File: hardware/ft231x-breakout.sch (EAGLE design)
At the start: 27 parts, among them Q1 2N7002PW, U1 FT231XS

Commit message: Silk Change
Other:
- note added: "V01"
- note removed: "V10"
- moved on the sheet: JP1, JP10, JP11

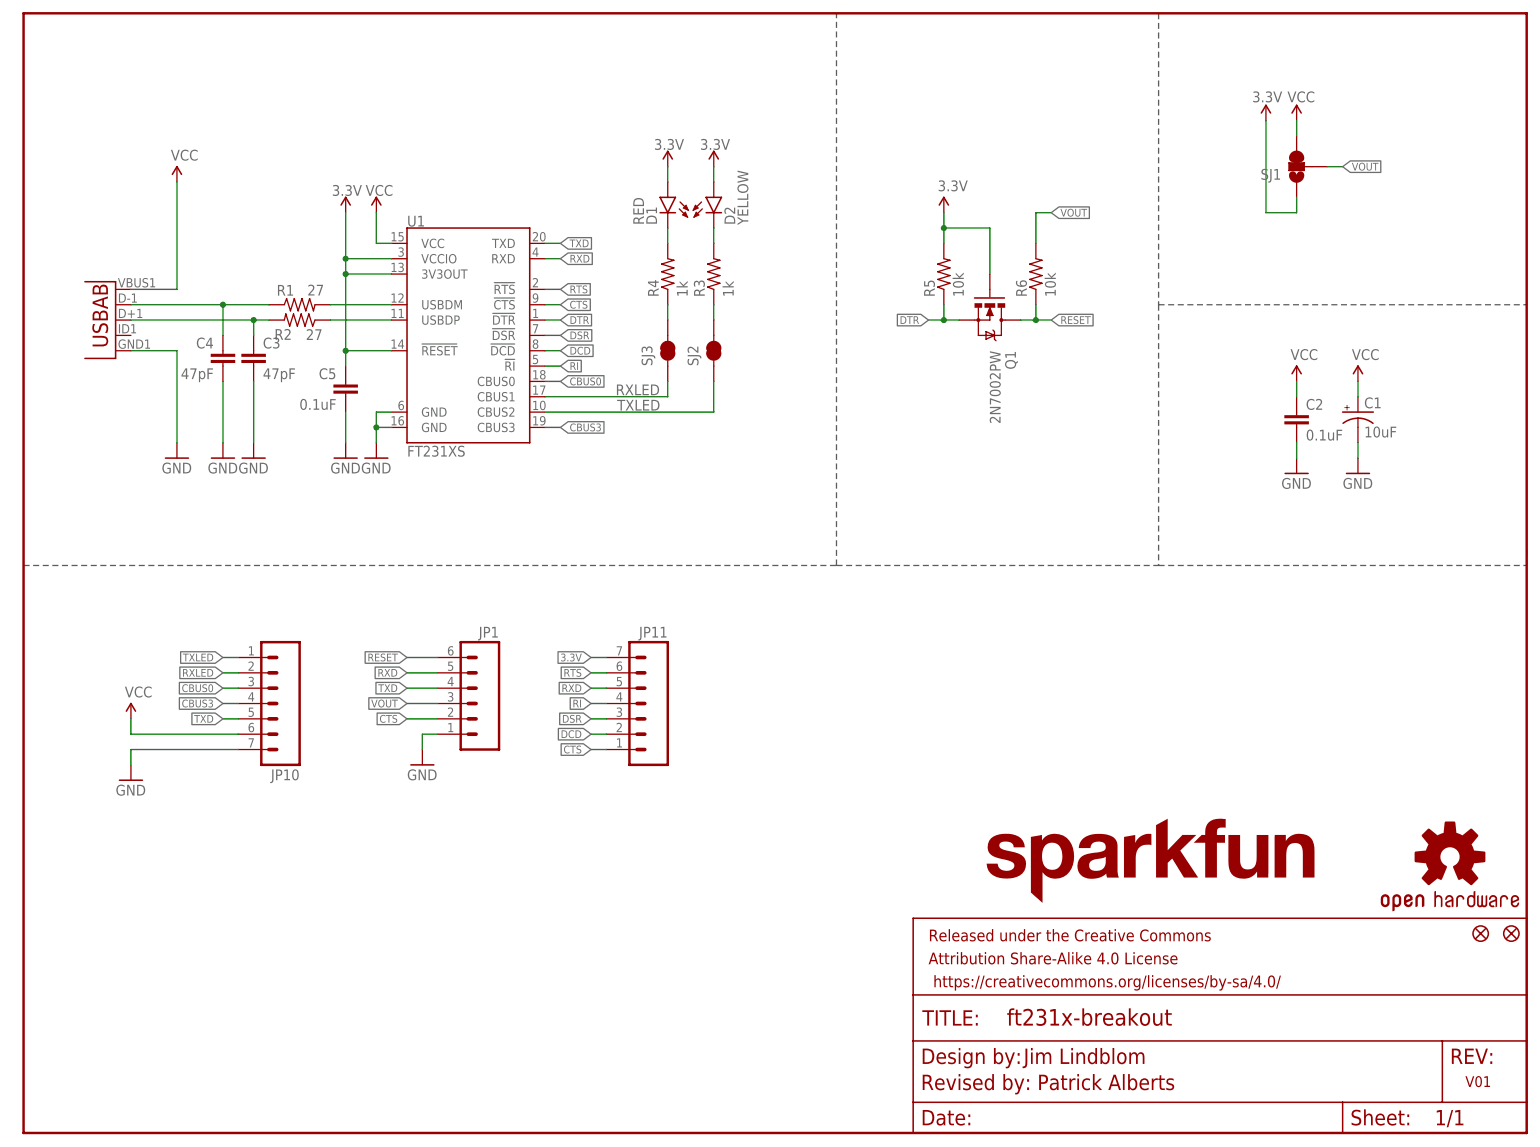
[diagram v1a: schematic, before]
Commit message: Adding sch notes, small silk edits, small trace fix
Adding notes for VIN and jumper usage. Also made some small silk edits
to avoid silk getting cut off by vias. Had to make one small trace
change on 3.3V net to avoid natural bridge between pads 13 and 14.
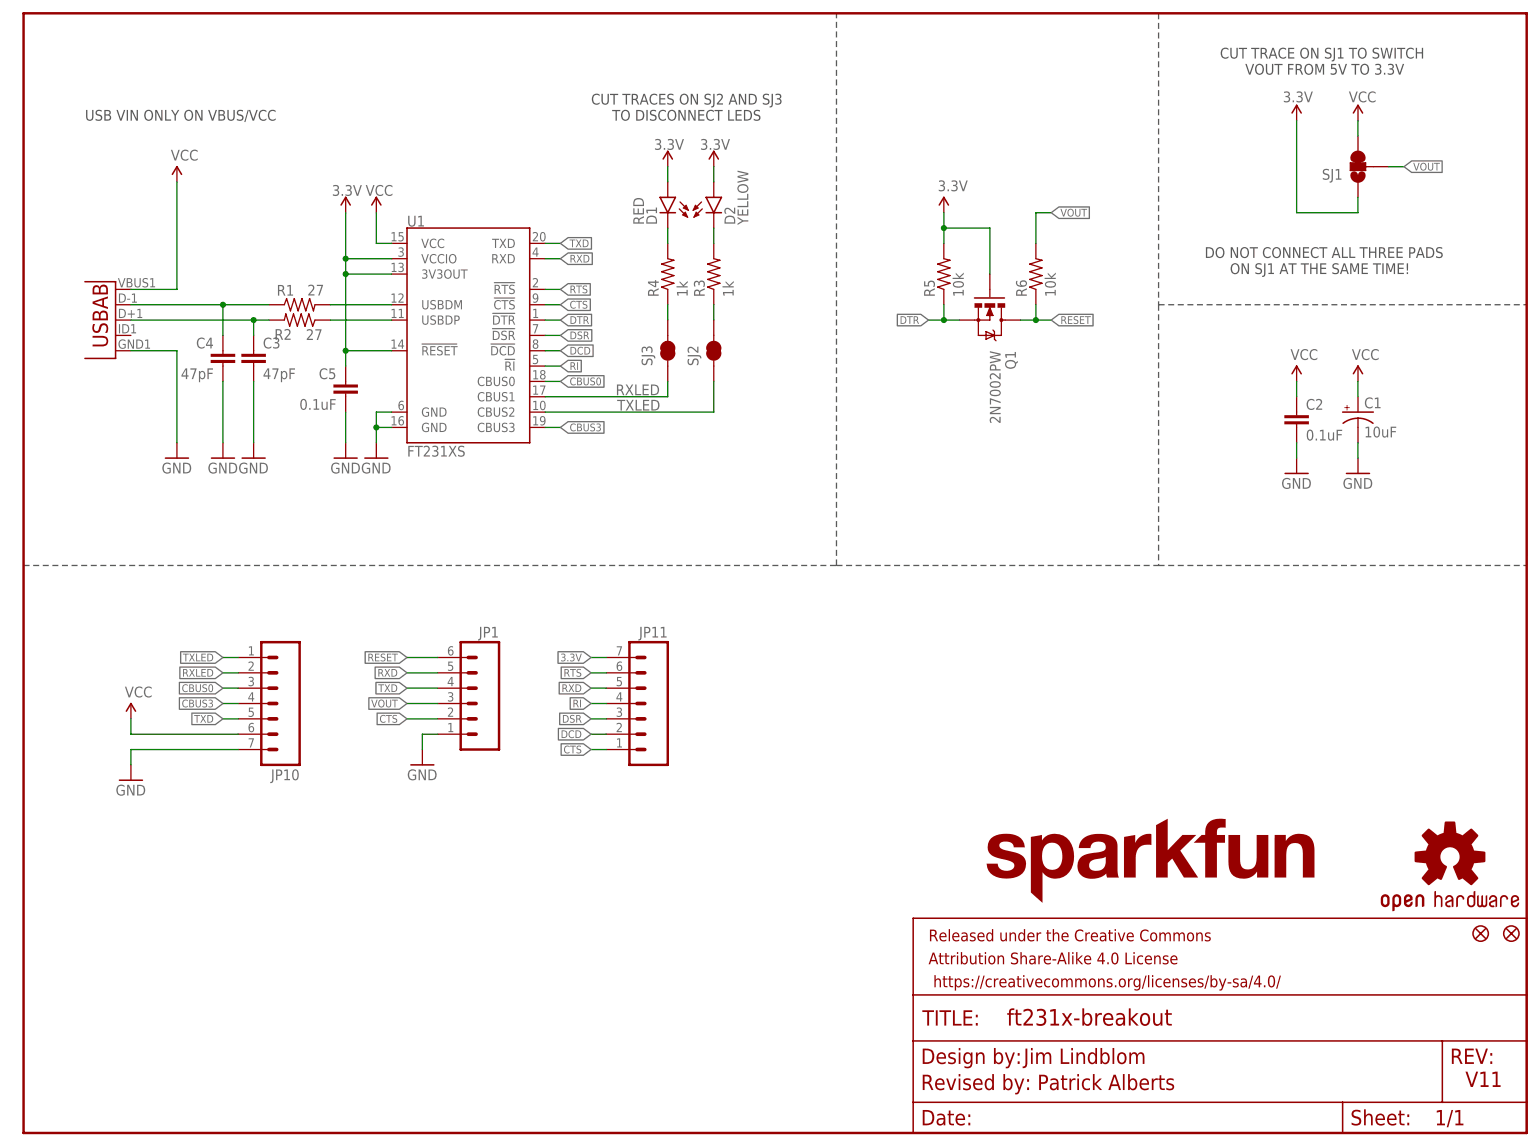
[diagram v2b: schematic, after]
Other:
- note added: "CUT TRACE ON SJ1 TO SWITCH VOUT FROM 5V TO 3.3V"
- note added: "CUT TRACES ON SJ2 AND SJ3 TO DISCONNECT LEDS"
- note added: "DO NOT CONNECT ALL THREE PADS ON SJ1 AT THE SAME TIME!"
- note added: "USB VIN ONLY ON VBUS/VCC"
- note added: "V11"
- note removed: "V01"
- moved on the sheet: SJ1
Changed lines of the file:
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@@
 <sheet>
 <plain>
-<wire x1="210.82" y1="160.02" x2="210.82" y2="161.798" width="1.016" layer="94"/>
+<wire x1="220.98" y1="160.02" x2="220.98" y2="161.798" width="1.016" layer="94"/>
 <wire x1="114.3" y1="128.778" x2="114.3" y2="130.302" width="1.016" layer="94"/>
 <wire x1="106.68" y1="128.778" x2="106.68" y2="130.302" width="1.016" layer="94"/>
@@
 <wire x1="187.96" y1="93.98" x2="248.92" y2="93.98" width="0.127" layer="97" style="shortdash"/>
 <wire x1="248.92" y1="93.98" x2="248.92" y2="96.52" width="0.127" layer="97" style="shortdash"/>
-<text x="238.76" y="7.62" size="1.778" layer="94">V01</text>
+<text x="238.76" y="7.62" size="2.54" layer="94">V11</text>
 <text x="165.608" y="11.43" size="2.54" layer="94">Jim Lindblom</text>
 <text x="148.59" y="7.112" size="2.54" layer="94">Revised by: Patrick Alberts</text>
 <wire x1="187.96" y1="137.16" x2="248.92" y2="137.16" width="0.127" layer="97" style="shortdash"/>
+<text x="10.16" y="167.64" size="1.778" layer="97">USB VIN ONLY ON VBUS/VCC</text>
+<text x="93.98" y="167.64" size="1.778" layer="97">CUT TRACES ON SJ2 AND SJ3
+     TO DISCONNECT LEDS</text>
+<text x="198.12" y="175.26" size="1.778" layer="97">CUT TRACE ON SJ1 TO SWITCH
+      VOUT FROM 5V TO 3.3V</text>
+<text x="195.58" y="142.24" size="1.778" layer="97">DO NOT CONNECT ALL THREE PADS
+      ON SJ1 AT THE SAME TIME!</text>
 </plain>
 <instances>
@@
 <instance part="JP1" gate="G$1" x="73.66" y="71.12" rot="MR0"/>
 <instance part="GND8" gate="1" x="66.04" y="60.96"/>
-<instance part="SJ1" gate="G$1" x="210.82" y="160.02" rot="R180"/>
+<instance part="SJ1" gate="G$1" x="220.98" y="160.02" rot="R180"/>
 <instance part="P+5" gate="G$1" x="53.34" y="152.4" smashed="yes">
 <attribute name="VALUE" x="51.054" y="155.194" size="1.778" layer="96"/>
 </instance>
-<instance part="P+6" gate="G$1" x="210.82" y="167.64" smashed="yes">
-<attribute name="VALUE" x="209.296" y="170.688" size="1.778" layer="96"/>
-</instance>
-<instance part="P+7" gate="G$1" x="205.74" y="167.64" smashed="yes">
-<attribute name="VALUE" x="203.454" y="170.688" size="1.778" layer="96"/>
+<instance part="P+6" gate="G$1" x="220.98" y="167.64" smashed="yes">
+<attribute name="VALUE" x="219.456" y="170.688" size="1.778" layer="96"/>
+</instance>
+<instance part="P+7" gate="G$1" x="210.82" y="167.64" smashed="yes">
+<attribute name="VALUE" x="208.534" y="170.688" size="1.778" layer="96"/>
 </instance>
 <instance part="P+1" gate="G$1" x="25.4" y="157.48"/>
@@
 <pinref part="SJ1" gate="G$1" pin="3"/>
 <pinref part="P+6" gate="G$1" pin="VCC"/>
-<wire x1="210.82" y1="167.64" x2="210.82" y2="165.1" width="0.1524" layer="91"/>
+<wire x1="220.98" y1="167.64" x2="220.98" y2="165.1" width="0.1524" layer="91"/>
 </segment>
 <segment>
@@
 <segment>
 <pinref part="SJ1" gate="G$1" pin="1"/>
-<wire x1="210.82" y1="154.94" x2="210.82" y2="152.4" width="0.1524" layer="91"/>
+<wire x1="220.98" y1="154.94" x2="220.98" y2="152.4" width="0.1524" layer="91"/>
 <pinref part="P+7" gate="G$1" pin="3.3V"/>
-<wire x1="210.82" y1="152.4" x2="205.74" y2="152.4" width="0.1524" layer="91"/>
-<wire x1="205.74" y1="152.4" x2="205.74" y2="167.64" width="0.1524" layer="91"/>
+<wire x1="220.98" y1="152.4" x2="210.82" y2="152.4" width="0.1524" layer="91"/>
+<wire x1="210.82" y1="152.4" x2="210.82" y2="167.64" width="0.1524" layer="91"/>
 </segment>
 <segment>
@@
 <segment>
 <pinref part="SJ1" gate="G$1" pin="2"/>
-<wire x1="215.9" y1="160.02" x2="218.44" y2="160.02" width="0.1524" layer="91"/>
-<label x="218.44" y="160.02" size="1.27" layer="95" xref="yes"/>
+<wire x1="226.06" y1="160.02" x2="228.6" y2="160.02" width="0.1524" layer="91"/>
+<label x="228.6" y="160.02" size="1.27" layer="95" xref="yes"/>
 </segment>
 <segment>
@@
 </schematic>
 </drawing>
+<compatibility>
+<note version="6.3" minversion="6.2.2" severity="warning">
+Since Version 6.2.2 text objects can contain more than one line,
+which will not be processed correctly with this version.
+</note>
+</compatibility>
 </eagle>

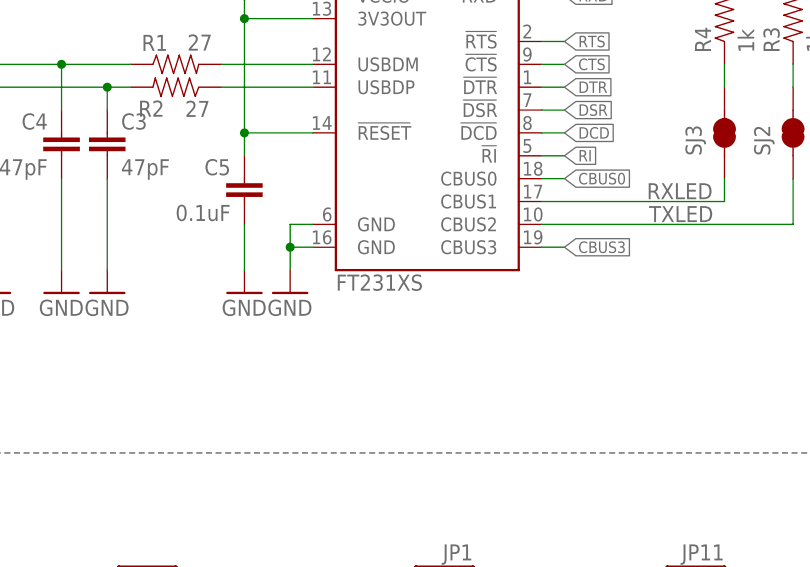
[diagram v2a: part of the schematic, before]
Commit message: Via drills change, moved R6 and library package update
Dropped all vias excepting the 3 usb connector staking vias to 15 mil to
jive better with silk. Moved R6 further in from edge of board to avoid
DPN damage/danger. Ran library update to include polarity mark silk
edits to SSOP20 package. Bumped micro-fiducials up to full fiducial
size.
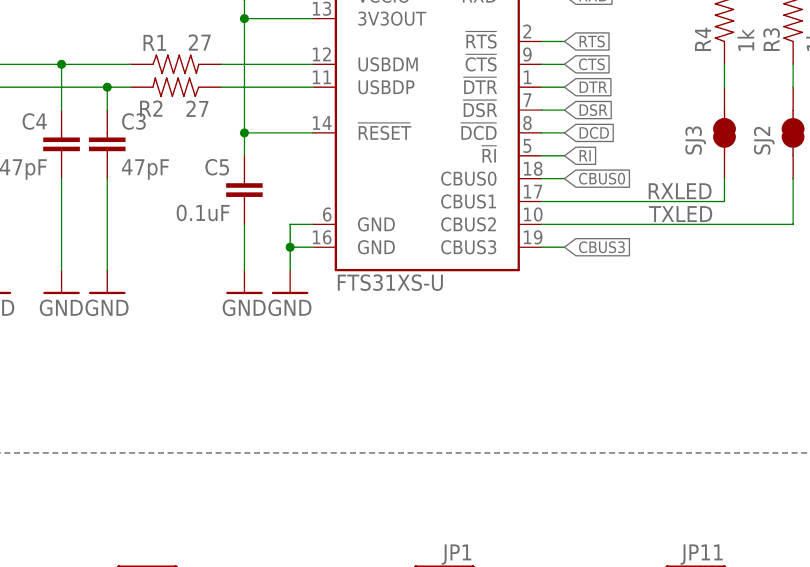
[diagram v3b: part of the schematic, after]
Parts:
- JP3, JP4: value FIDUCIALUFIDUCIAL -> FIDUCIAL1X2; device SparkFun-Aesthetics:FIDUCIALUFIDUCIAL -> SparkFun-Aesthetics:FIDUCIAL1X2
- U1: value FT231XS -> FTS31XS-U

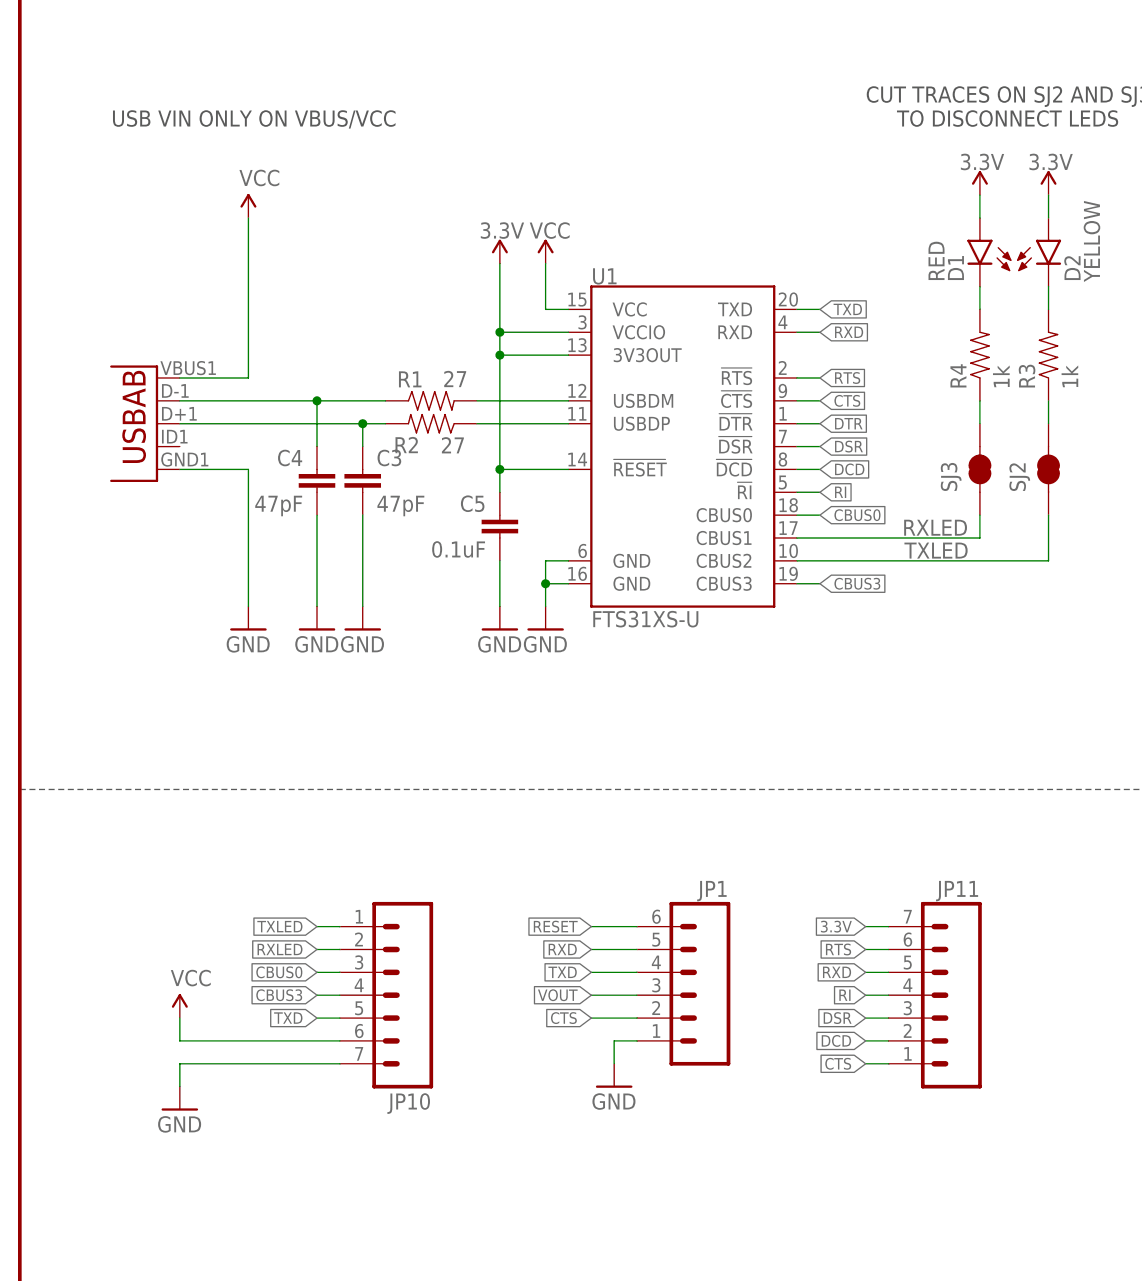
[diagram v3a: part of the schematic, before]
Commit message: Fixing issues from design checklist
See issue #4 in repo for full rundown.
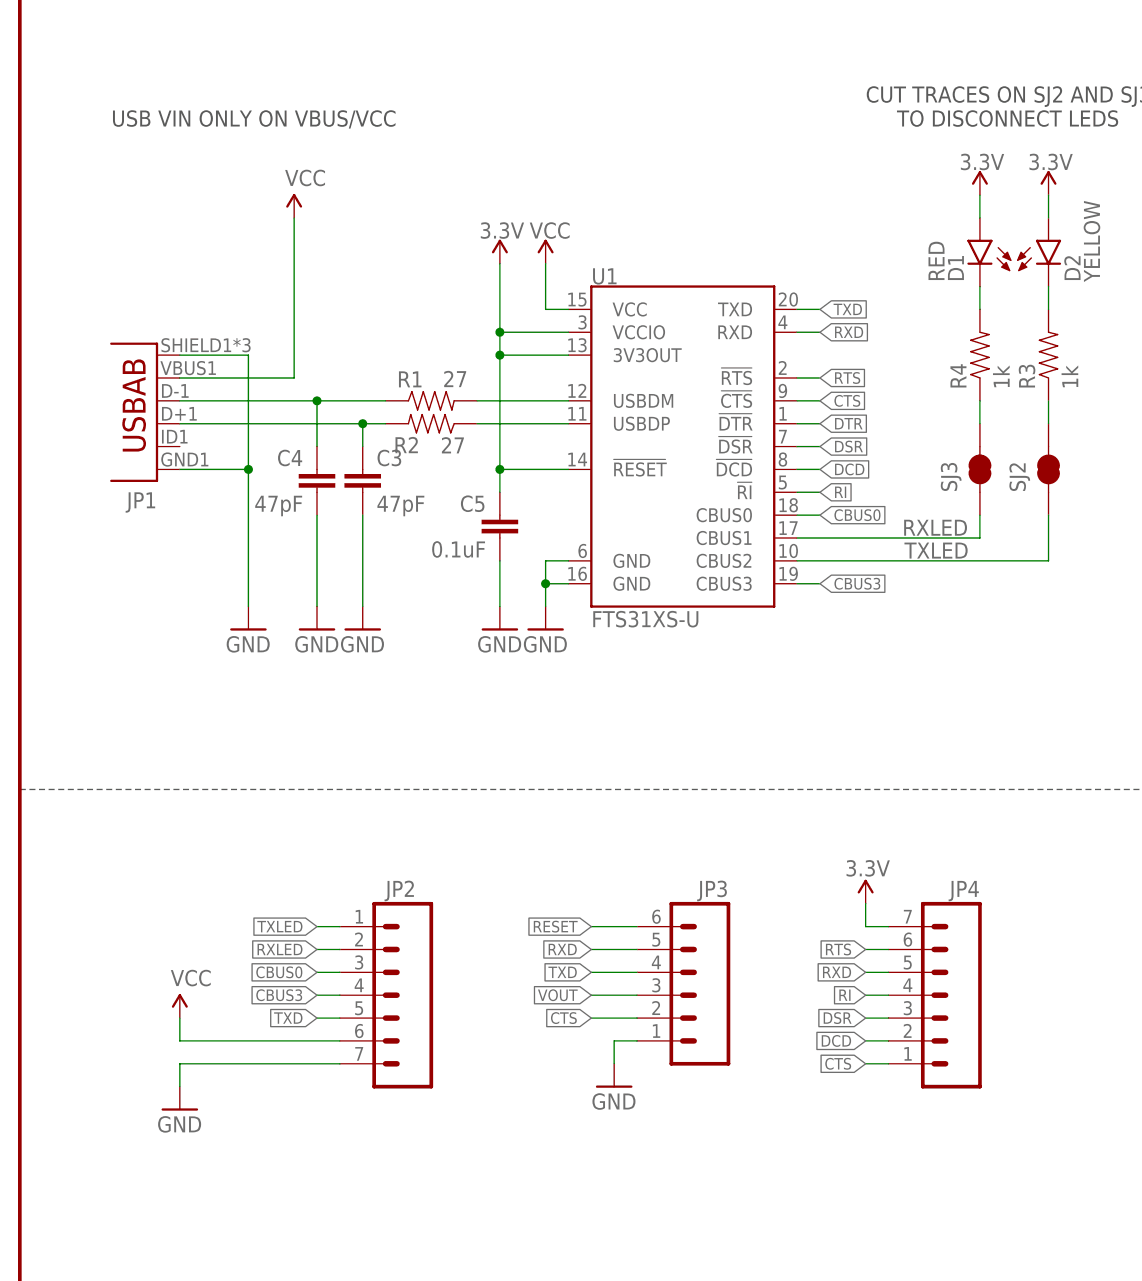
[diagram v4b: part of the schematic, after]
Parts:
- removed JP11: (no value), SparkFun-Connectors:M07NS
- removed X1: (no value), SparkFun-Connectors:USB-ABCONN-11794
- added JP5, JP6: FIDUCIAL1X2, SparkFun-Aesthetics:FIDUCIAL1X2
- JP1: device SparkFun-Connectors:M06SIP-NS -> SparkFun-Connectors:USB-ABCONN-11794
- JP3: value FIDUCIAL1X2 -> (none); device SparkFun-Aesthetics:FIDUCIAL1X2 -> SparkFun-Connectors:M06SIP-NS
- JP4: value FIDUCIAL1X2 -> (none); device SparkFun-Aesthetics:FIDUCIAL1X2 -> SparkFun-Connectors:M07NS
- renumbered JP10 to JP2
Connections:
- net 3.3V: now also JP4.7; no longer JP11.7
- net CTS: now also JP3.2, JP4.1; no longer JP1.2, JP11.1
- net DCD: now also JP4.2; no longer JP11.2
- net DSR: now also JP4.3; no longer JP11.3
- net GND: now also JP1.GND, JP1.SHIELD, JP3.1; no longer JP1.1, X1.GND
- net N$3: now also JP1.D+; no longer X1.D+
- net N$4: now also JP1.D-; no longer X1.D-
- net RESET: now also JP3.6; no longer JP1.6
- net RI: now also JP4.4; no longer JP11.4
- net RTS: now also JP4.6; no longer JP11.6
- net RXD: now also JP3.5, JP4.5; no longer JP1.5, JP11.5
- net TXD: now also JP3.4; no longer JP1.4
- net VCC: now also JP1.VBUS; no longer X1.VBUS
- net VOUT: now also JP3.3; no longer JP1.3
